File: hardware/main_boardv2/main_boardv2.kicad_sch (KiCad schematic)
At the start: 4 parts

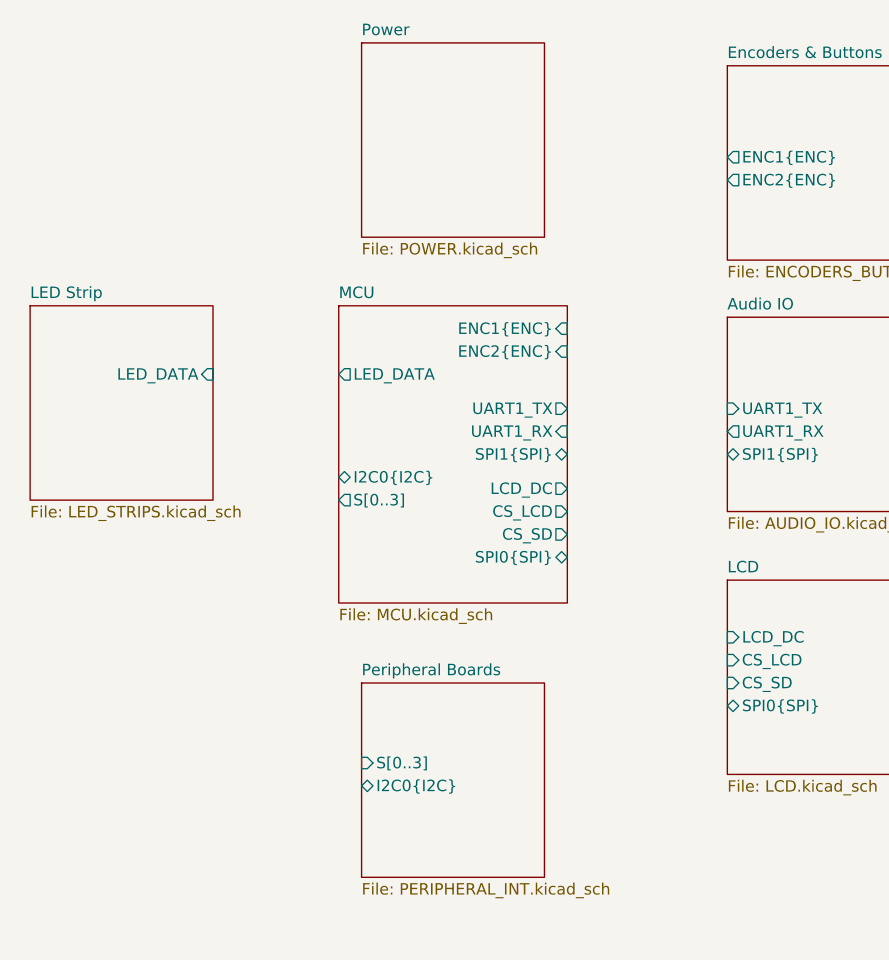
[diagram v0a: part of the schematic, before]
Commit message: wired most of new hardware. need to reviist audio stuff
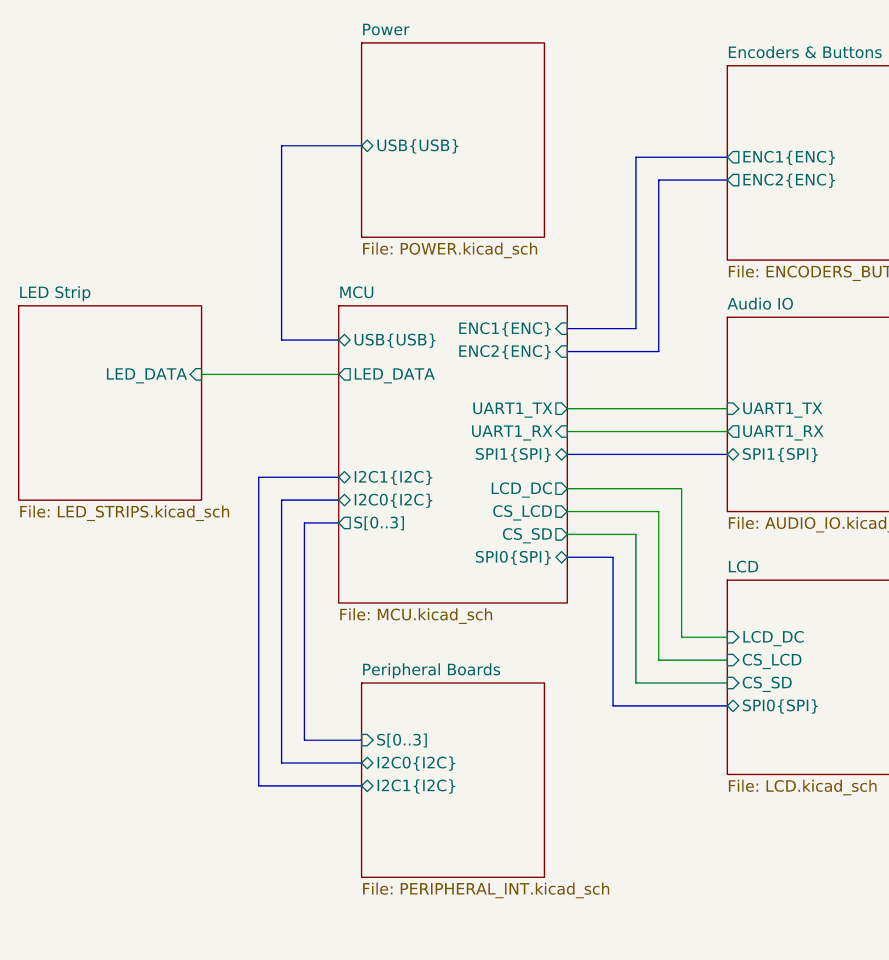
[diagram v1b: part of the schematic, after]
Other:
- sheet MCU ports: added I2C1{I2C}, USB{USB}; removed none
- sheet Peripheral Boards ports: added I2C1{I2C}; removed none
- sheet Power ports: added USB{USB}; removed none
